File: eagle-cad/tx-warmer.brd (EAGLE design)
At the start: 44.5 x 44.5 mm, 22 parts, among them IC2 MCP1702

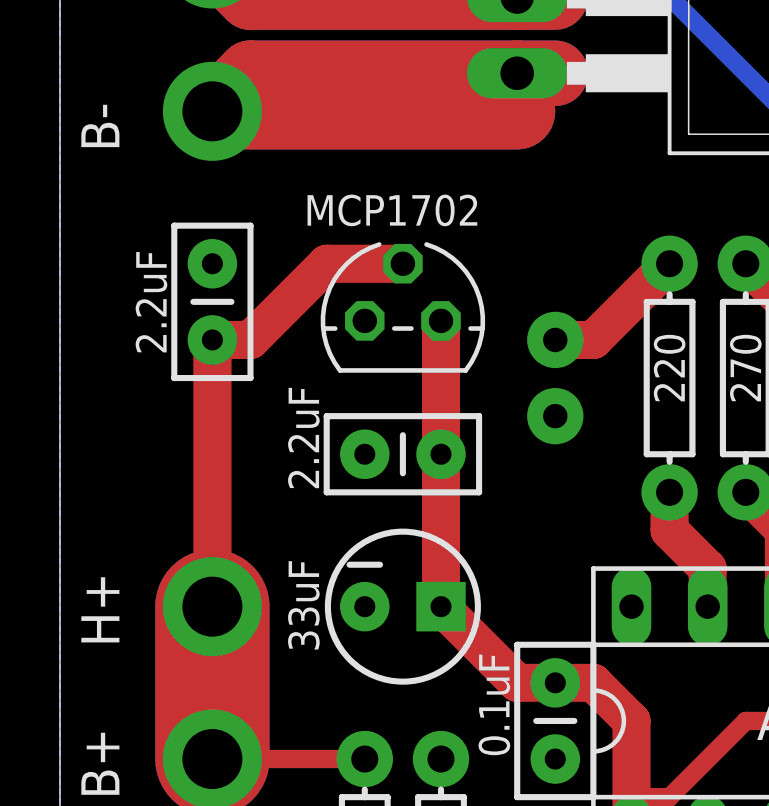
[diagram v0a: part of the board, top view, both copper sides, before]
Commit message: Changed voltage regulator MCP1702 to LP2950 (formed leads)
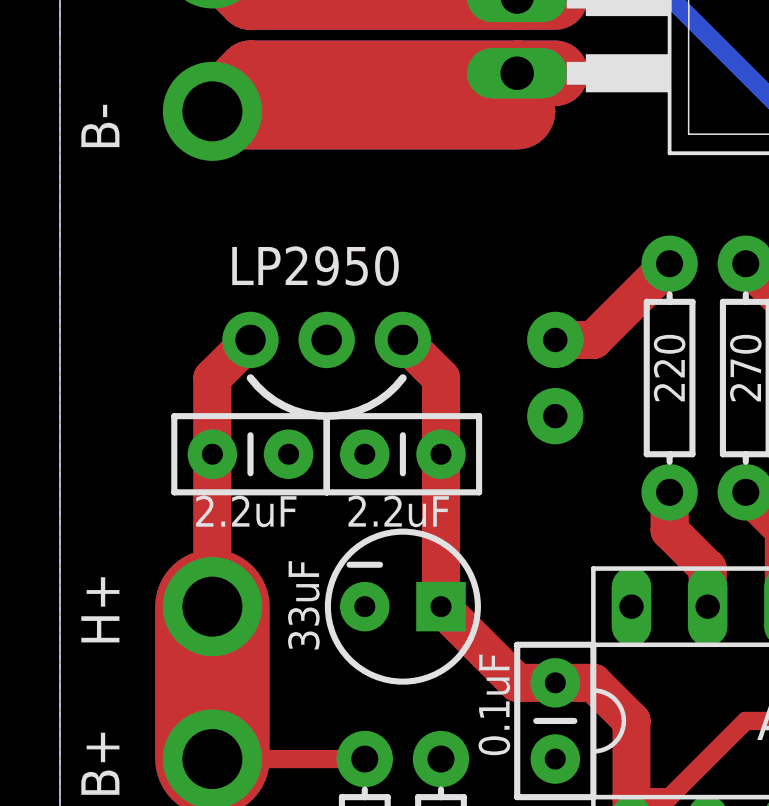
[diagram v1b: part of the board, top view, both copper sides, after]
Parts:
- removed IC2: MCP1702, linear:TO92
- added LP2950: (no value), SparkFun-Connectors:1X03_NO_SILK
- moved C2 3.81 mm to (3.81, 20.3), turned to 0 degrees
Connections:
- net 5V: now also LP2950.3; no longer IC2.3
- net GND: now also LP2950.2; no longer IC2.1
- net N$4: now also LP2950.1; no longer IC2.2
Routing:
- net N$4: track 31.5 -> 24.7 mm
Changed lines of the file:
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@@
 <text x="19.05" y="13.335" size="1.27" layer="22" rot="MR180">TX-warmer v1.4</text>
 <text x="16.51" y="10.795" size="1.27" layer="22" rot="MR180">Pertti Erkkilä 2012</text>
+<wire x1="10.16" y1="22.86" x2="5.08" y2="22.86" width="0.254" layer="21" curve="-106.260205"/>
 </plain>
 <attributes>
@@
 <attribute name="NAME" x="24.257" y="39.37" size="1.016" layer="25" ratio="10" rot="R270"/>
 </element>
-<element name="IC2" library="linear" package="TO92" value="MCP1702" x="10.16" y="24.765" smashed="yes">
-<attribute name="VALUE" x="6.858" y="27.94" size="1.016" layer="21" ratio="10"/>
-</element>
 <element name="SWITCH" library="SparkFun-Electromechanical" package="TACTILE-PTH" value="" x="36.83" y="22.86" smashed="yes" rot="MR180"/>
 <element name="R9" library="SparkFun-Resistors" package="AXIAL-0.3EZ" value="270" x="21.59" y="22.86" smashed="yes" rot="R270">
@@
 </element>
 <element name="C1" library="SparkFun-Passives" package="CAP-PTH-SMALLEZ" value="2.2uF" x="11.43" y="20.32" smashed="yes" rot="R180">
-<attribute name="VALUE" x="6.35" y="22.606" size="1.016" layer="21" rot="R270"/>
-</element>
-<element name="C2" library="SparkFun-Passives" package="CAP-PTH-SMALLEZ" value="2.2uF" x="3.81" y="24.13" smashed="yes" rot="R90">
-<attribute name="VALUE" x="2.286" y="23.622" size="1.016" layer="21" rot="R90"/>
+<attribute name="VALUE" x="8.255" y="17.907" size="1.016" layer="21"/>
+</element>
+<element name="C2" library="SparkFun-Passives" package="CAP-PTH-SMALLEZ" value="2.2uF" x="3.81" y="20.32" smashed="yes">
+<attribute name="VALUE" x="3.175" y="17.907" size="1.016" layer="21"/>
 </element>
 <element name="C3" library="SparkFun-Passives" package="CAP-PTH-SMALLEZ" value="0.1uF" x="15.24" y="12.7" smashed="yes" rot="R270">
@@
 <element name="H-" library="SparkFun-Connectors" package="1X01_2MM" value="M01PTH_2MM" x="3.81" y="36.83" smashed="yes">
 <attribute name="NAME" x="0.7112" y="35.4838" size="1.27" layer="25" rot="R90"/>
+</element>
+<element name="LP2950" library="SparkFun-Connectors" package="1X03_NO_SILK" value="" x="5.08" y="24.13" smashed="yes">
+<attribute name="NAME" x="4.318" y="25.9588" size="1.27" layer="25" ratio="10"/>
+<attribute name="VALUE" x="3.81" y="20.955" size="1.27" layer="27"/>
 </element>
 </elements>
@@
 <signal name="N$4">
 <contactref element="R3" pad="P$1"/>
-<contactref element="IC2" pad="2"/>
 <contactref element="C2" pad="1"/>
-<wire x1="10.16" y1="26.67" x2="7.62" y2="26.67" width="1.27" layer="1"/>
-<wire x1="7.62" y1="26.67" x2="5.08" y2="24.13" width="1.27" layer="1"/>
-<wire x1="5.08" y1="24.13" x2="3.81" y2="24.13" width="1.27" layer="1"/>
 <contactref element="B+" pad="1"/>
 <contactref element="H+" pad="1"/>
@@
 <wire x1="3.81" y1="10.16" x2="3.81" y2="15.24" width="3.81" layer="1"/>
 <wire x1="8.89" y1="10.16" x2="3.81" y2="10.16" width="0.6096" layer="1"/>
-<wire x1="3.81" y1="24.13" x2="3.81" y2="15.24" width="1.27" layer="1"/>
+<wire x1="3.81" y1="20.32" x2="3.81" y2="15.24" width="1.27" layer="1"/>
+<contactref element="LP2950" pad="1"/>
+<wire x1="3.81" y1="20.32" x2="3.81" y2="22.86" width="1.27" layer="1"/>
+<wire x1="3.81" y1="22.86" x2="5.08" y2="24.13" width="1.27" layer="1"/>
 </signal>
 <signal name="GND">
@@
 <contactref element="LED2" pad="K"/>
 <contactref element="LED1" pad="K"/>
-<contactref element="IC2" pad="1"/>
 <contactref element="ISP" pad="4"/>
 <contactref element="C5" pad="2"/>
@@
 <wire x1="13.97" y1="33.02" x2="15.24" y2="33.02" width="2.1844" layer="1"/>
 <wire x1="3.81" y1="31.75" x2="13.97" y2="31.75" width="2.54" layer="16"/>
+<contactref element="LP2950" pad="2"/>
 </signal>
 <signal name="5V">
@@
 <contactref element="ISP" pad="3"/>
 <wire x1="17.78" y1="7.62" x2="19.05" y2="8.89" width="0.6096" layer="1"/>
-<contactref element="IC2" pad="3"/>
 <contactref element="C5" pad="1"/>
 <contactref element="C1" pad="1"/>
@@
 <wire x1="17.78" y1="5.08" x2="17.78" y2="7.62" width="0.6096" layer="1"/>
 <wire x1="19.05" y1="8.89" x2="17.78" y2="8.89" width="0.6096" layer="1"/>
-<wire x1="11.43" y1="24.765" x2="11.43" y2="20.32" width="1.27" layer="1"/>
 <wire x1="11.43" y1="20.32" x2="11.43" y2="15.24" width="1.27" layer="1"/>
 <wire x1="17.78" y1="7.62" x2="17.78" y2="8.89" width="1.27" layer="1"/>
@@
 <wire x1="35.56" y1="11.43" x2="36.83" y2="10.16" width="0.6096" layer="1"/>
 <wire x1="36.83" y1="10.16" x2="38.1" y2="10.16" width="0.6096" layer="1"/>
+<contactref element="LP2950" pad="3"/>
+<wire x1="11.43" y1="20.32" x2="11.43" y2="22.86" width="1.27" layer="1"/>
+<wire x1="11.43" y1="22.86" x2="10.16" y2="24.13" width="1.27" layer="1"/>
 </signal>
 <signal name="N$6">

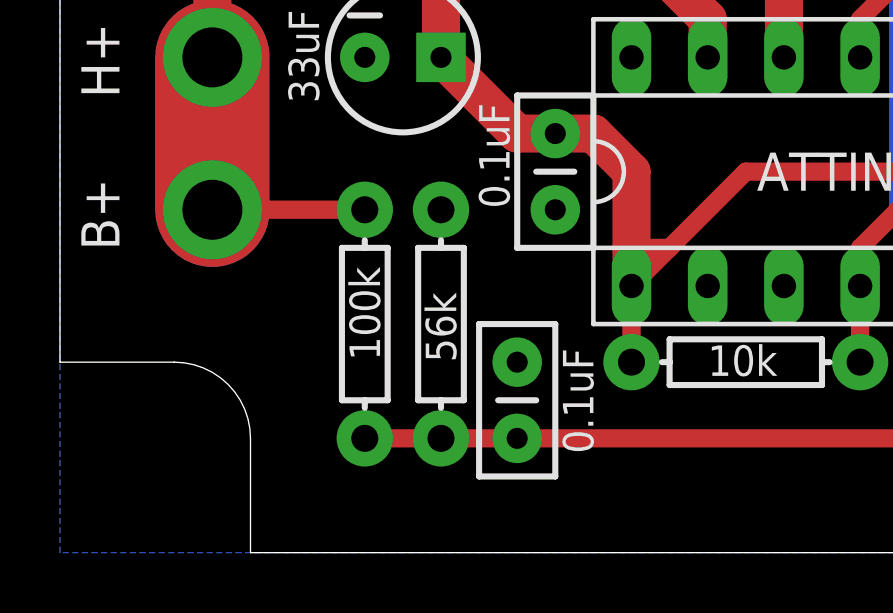
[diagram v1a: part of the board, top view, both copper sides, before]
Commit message: Modified voltage divider to support higher voltages (max now 20.1V)
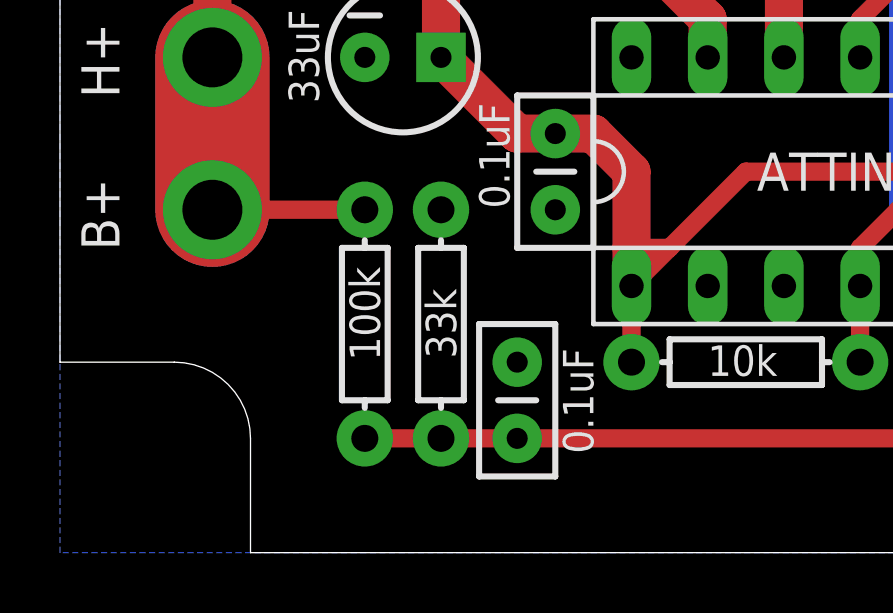
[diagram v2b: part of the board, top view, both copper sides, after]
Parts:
- R4: value 56k -> 33k
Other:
- board text added: "TX-warmer v1.5"
- board text removed: "TX-warmer v1.4"
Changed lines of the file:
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@@
 <hole x="8.4582" y="40.2082" drill="2.54"/>
 <hole x="33.4518" y="1.7018" drill="2.54"/>
-<text x="19.05" y="13.335" size="1.27" layer="22" rot="MR180">TX-warmer v1.4</text>
+<text x="19.05" y="13.335" size="1.27" layer="22" rot="MR180">TX-warmer v1.5</text>
 <text x="16.51" y="10.795" size="1.27" layer="22" rot="MR180">Pertti Erkkilä 2012</text>
 <wire x1="10.16" y1="22.86" x2="5.08" y2="22.86" width="0.254" layer="21" curve="-106.260205"/>
@@
 <attribute name="VALUE" x="8.382" y="8.255" size="1.016" layer="21" font="vector" ratio="15" rot="R270"/>
 </element>
-<element name="R4" library="SparkFun-Resistors" package="AXIAL-0.3EZ" value="56k" x="11.43" y="6.35" smashed="yes" rot="R90">
-<attribute name="VALUE" x="11.938" y="5.08" size="1.016" layer="21" font="vector" ratio="15" rot="R90"/>
+<element name="R4" library="SparkFun-Resistors" package="AXIAL-0.3EZ" value="33k" x="11.43" y="6.35" smashed="yes" rot="R90">
+<attribute name="VALUE" x="11.938" y="5.207" size="1.016" layer="21" font="vector" ratio="15" rot="R90"/>
 </element>
 <element name="LED1" library="SparkFun-LED" package="LED5MM-KIT" value="GREEN" x="15.24" y="22.86" smashed="yes" rot="MR270">

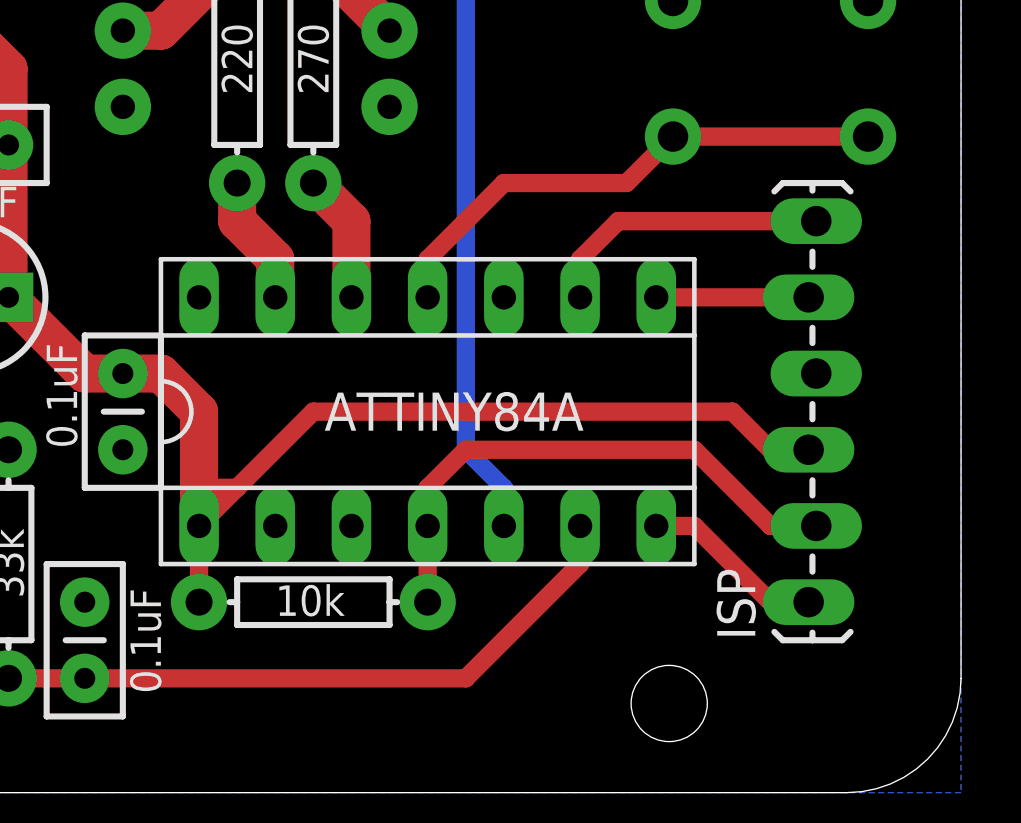
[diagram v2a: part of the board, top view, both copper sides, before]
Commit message: Removed ISP-header. Mainly useless and made room for future changes
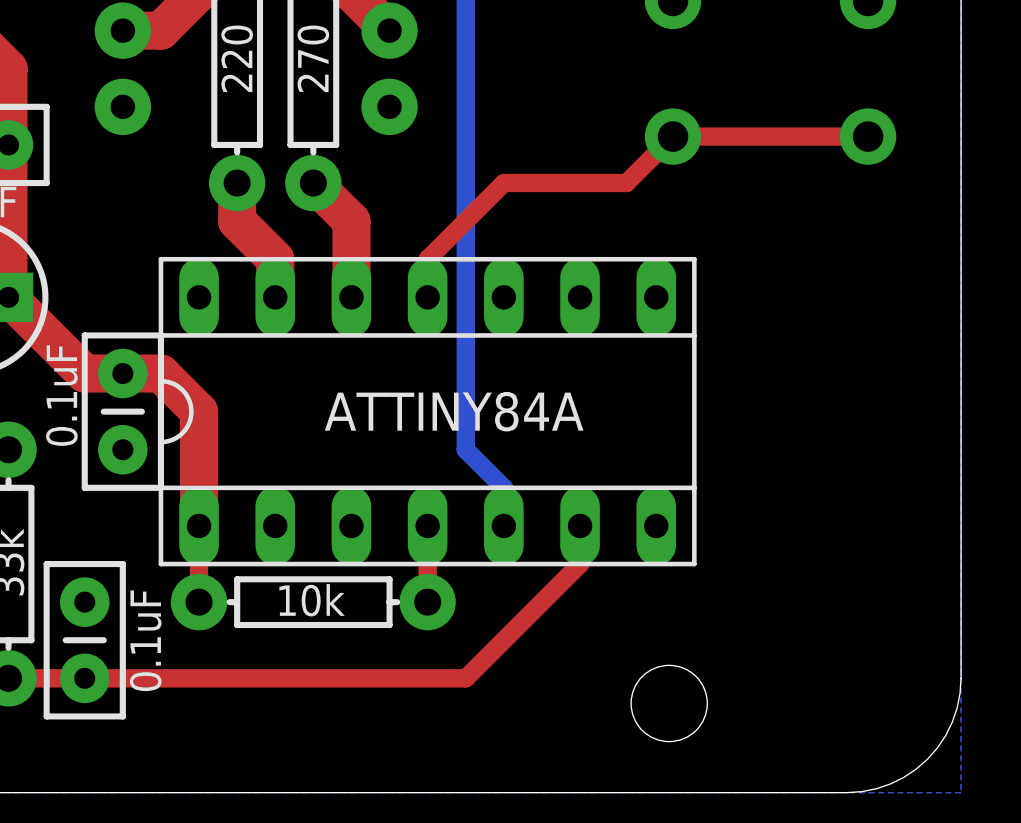
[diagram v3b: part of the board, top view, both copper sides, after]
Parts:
- removed ISP: (no value), SparkFun-Connectors:1X06_LOCK_LONGPADS
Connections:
- removed net N$2: ATTINY84A.8, ISP.5
- removed net N$3: ATTINY84A.7, ISP.1
- removed net N$5: ATTINY84A.9, ISP.6
- net 5V: no longer ISP.3
- net GND: no longer ISP.4
- net N$11: no longer ISP.2
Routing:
- net 5V: track 47.4 -> 23.7 mm
- net N$11: track 18.3 -> 2.54 mm
- net N$5: track 9.67 -> 0.00 mm
- net N$3: track 6.13 -> 0.00 mm
- net N$2: track 5.08 -> 0.00 mm
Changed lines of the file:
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@@
 <attribute name="VALUE" x="22.2504" y="19.5834" size="1.27" layer="22" ratio="10" rot="MR180"/>
 </element>
-<element name="ISP" library="SparkFun-Connectors" package="1X06_LOCK_LONGPADS" value="" x="38.1" y="5.08" rot="R90"/>
 <element name="C5" library="SparkFun-Capacitors" package="CPOL-RADIAL-10UF-25V" value="33uF" x="10.16" y="15.24" smashed="yes">
 <attribute name="VALUE" x="7.366" y="13.716" size="1.016" layer="21" rot="R90"/>
@@
 <contactref element="LED2" pad="K"/>
 <contactref element="LED1" pad="K"/>
-<contactref element="ISP" pad="4"/>
 <contactref element="C5" pad="2"/>
 <contactref element="C6" pad="2"/>
@@
 <signal name="5V">
 <contactref element="ATTINY84A" pad="1"/>
-<contactref element="ISP" pad="3"/>
-<wire x1="17.78" y1="7.62" x2="19.05" y2="8.89" width="0.6096" layer="1"/>
 <contactref element="C5" pad="1"/>
 <contactref element="C1" pad="1"/>
@@
 <contactref element="R1" pad="P$1"/>
 <wire x1="17.78" y1="5.08" x2="17.78" y2="7.62" width="0.6096" layer="1"/>
-<wire x1="19.05" y1="8.89" x2="17.78" y2="8.89" width="0.6096" layer="1"/>
 <wire x1="11.43" y1="20.32" x2="11.43" y2="15.24" width="1.27" layer="1"/>
-<wire x1="17.78" y1="7.62" x2="17.78" y2="8.89" width="1.27" layer="1"/>
 <wire x1="15.24" y1="12.7" x2="13.97" y2="12.7" width="1.27" layer="1"/>
 <wire x1="13.97" y1="12.7" x2="11.43" y2="15.24" width="1.27" layer="1"/>
-<wire x1="17.78" y1="8.89" x2="17.78" y2="11.43" width="1.27" layer="1"/>
+<wire x1="17.78" y1="7.62" x2="17.78" y2="11.43" width="1.27" layer="1"/>
 <wire x1="17.78" y1="11.43" x2="16.51" y2="12.7" width="1.27" layer="1"/>
 <wire x1="16.51" y1="12.7" x2="15.24" y2="12.7" width="1.27" layer="1"/>
-<wire x1="19.05" y1="8.89" x2="21.59" y2="11.43" width="0.6096" layer="1"/>
-<wire x1="21.59" y1="11.43" x2="35.56" y2="11.43" width="0.6096" layer="1"/>
-<wire x1="35.56" y1="11.43" x2="36.83" y2="10.16" width="0.6096" layer="1"/>
-<wire x1="36.83" y1="10.16" x2="38.1" y2="10.16" width="0.6096" layer="1"/>
 <contactref element="LP2950" pad="3"/>
 <wire x1="11.43" y1="20.32" x2="11.43" y2="22.86" width="1.27" layer="1"/>
@@
 <signal name="N$16">
 </signal>
-<signal name="N$2">
-<contactref element="ATTINY84A" pad="8"/>
-<contactref element="ISP" pad="5"/>
-<wire x1="33.02" y1="15.24" x2="38.1" y2="15.24" width="0.6096" layer="1"/>
-</signal>
-<signal name="N$3">
-<contactref element="ATTINY84A" pad="7"/>
-<contactref element="ISP" pad="1"/>
-<wire x1="38.1" y1="5.08" x2="36.83" y2="5.08" width="0.6096" layer="1"/>
-<wire x1="36.83" y1="5.08" x2="34.29" y2="7.62" width="0.6096" layer="1"/>
-<wire x1="34.29" y1="7.62" x2="33.02" y2="7.62" width="0.6096" layer="1"/>
-</signal>
-<signal name="N$5">
-<contactref element="ATTINY84A" pad="9"/>
-<contactref element="ISP" pad="6"/>
-<wire x1="30.48" y1="15.24" x2="30.48" y2="16.51" width="0.6096" layer="1"/>
-<wire x1="30.48" y1="16.51" x2="31.75" y2="17.78" width="0.6096" layer="1"/>
-<wire x1="31.75" y1="17.78" x2="38.354" y2="17.78" width="0.6096" layer="1"/>
-</signal>
 <signal name="N$11">
 <contactref element="ATTINY84A" pad="4"/>
-<contactref element="ISP" pad="2"/>
-<wire x1="36.83" y1="7.62" x2="38.354" y2="7.62" width="0.6096" layer="1"/>
 <contactref element="R1" pad="P$2"/>
 <wire x1="25.4" y1="5.08" x2="25.4" y2="7.62" width="0.6096" layer="1"/>
-<wire x1="36.83" y1="7.62" x2="34.29" y2="10.16" width="0.6096" layer="1"/>
-<wire x1="34.29" y1="10.16" x2="26.67" y2="10.16" width="0.6096" layer="1"/>
-<wire x1="26.67" y1="10.16" x2="25.4" y2="8.89" width="0.6096" layer="1"/>
-<wire x1="25.4" y1="8.89" x2="25.4" y2="7.62" width="0.6096" layer="1"/>
 </signal>
 <signal name="N$12">
